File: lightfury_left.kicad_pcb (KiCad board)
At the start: 6 copper layers, 156 x 116.5 mm, 89 parts, among them U1 TLV61070ADBV, U2 SN74LV1T126DBVR

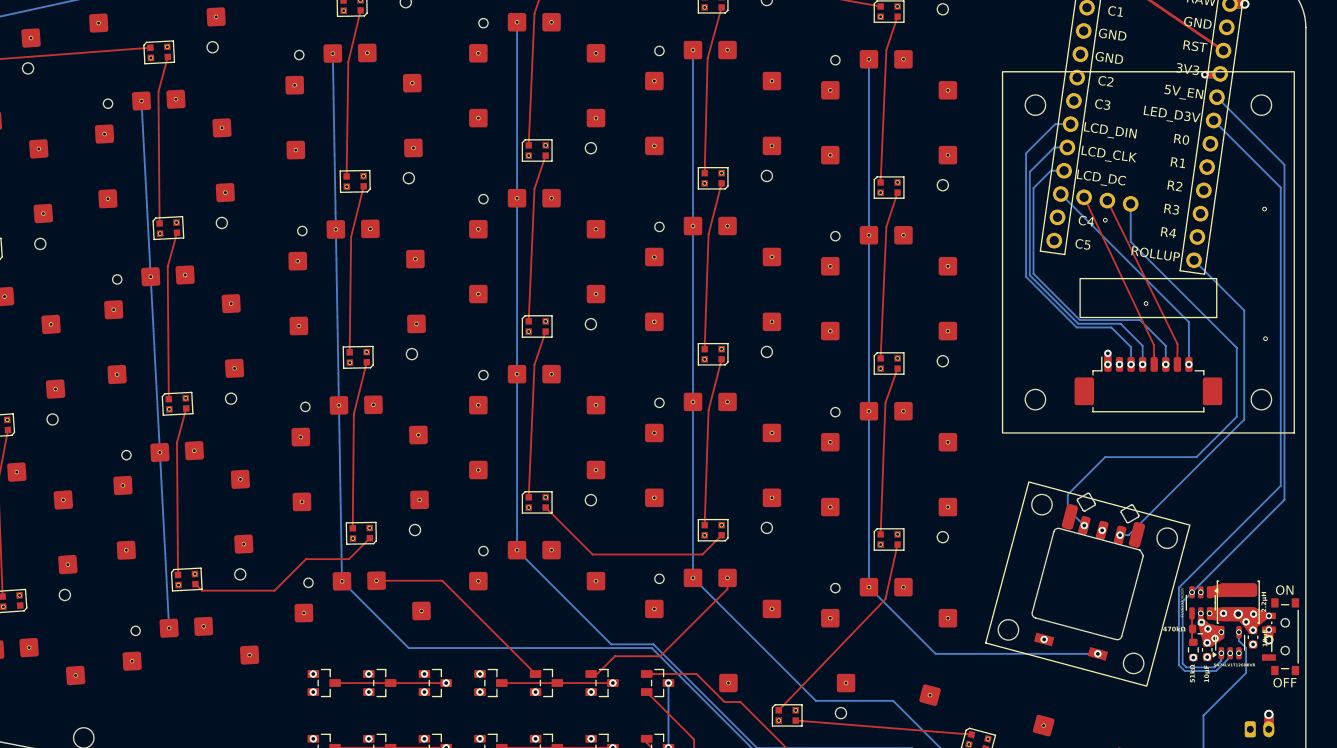
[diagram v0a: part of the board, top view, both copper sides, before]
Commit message: Added capacitors for 5v load smoothing.
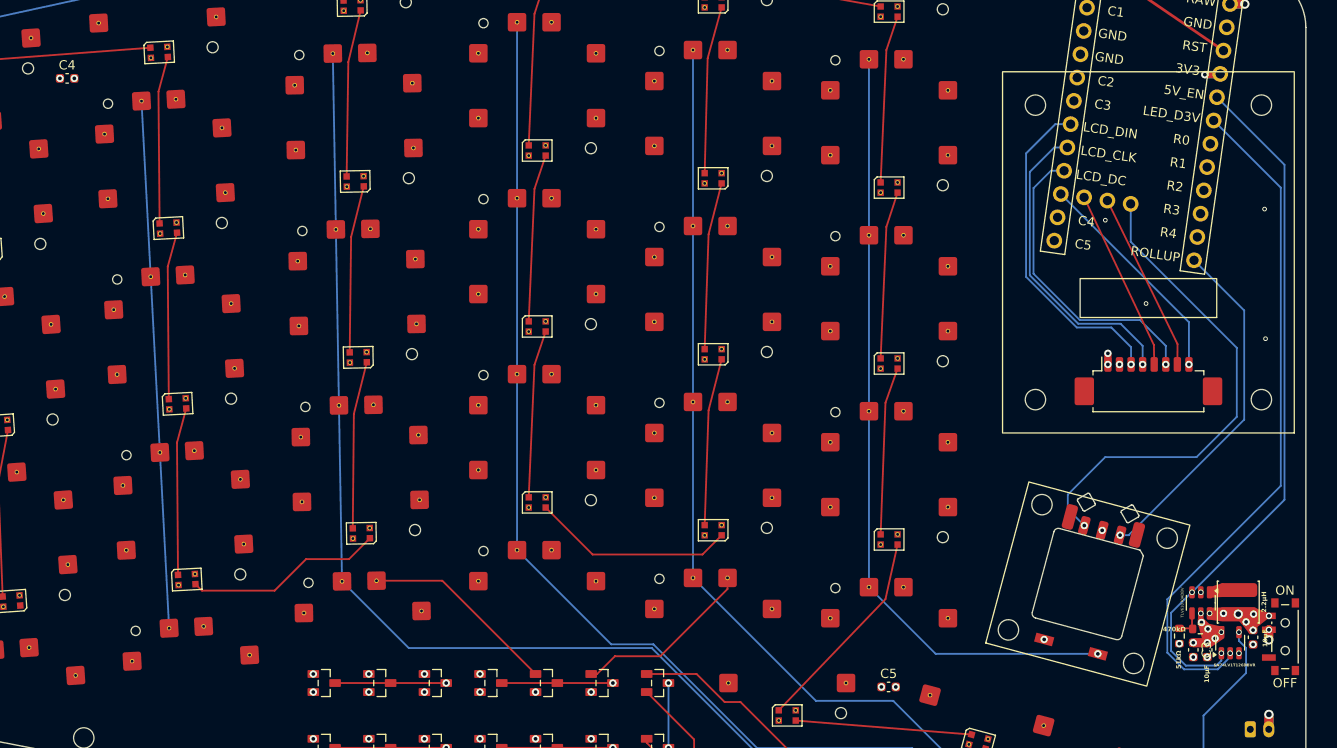
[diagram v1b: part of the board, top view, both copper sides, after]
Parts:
- added C3: 100nF, Capacitor_SMD:C_0603_1608Metric, F.Cu at (191.8, 202.2)
- added C4: 10µF, Capacitor_SMD:C_0603_1608Metric, F.Cu at (70.2, 140.5)
- added C5: 10µF, Capacitor_SMD:C_0603_1608Metric, F.Cu at (158.9, 206.2)
- moved R2 2.13 mm to (190.3, 200.7)
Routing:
- net 5V: track 4.02 -> 7.42 mm, vias 6 -> 9
- net 5V_EN: track 74.2 -> 75.0 mm
- net LED_D3V: track 73.2 -> 74.0 mm
- net GND: vias 13 -> 16

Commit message: Add LCSC field and populate for BOM.
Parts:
- C2: value 10μF -> 10μF 25V
- C4, C5: value 10µF -> 10µF 25V
